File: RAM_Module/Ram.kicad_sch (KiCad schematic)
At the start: 10 parts, among them SW3 SW_Push, U3 74LS00, U4 74LS157, U5 74F189SC, U6 74F189SC, U7 74LS157, U8 74LS157

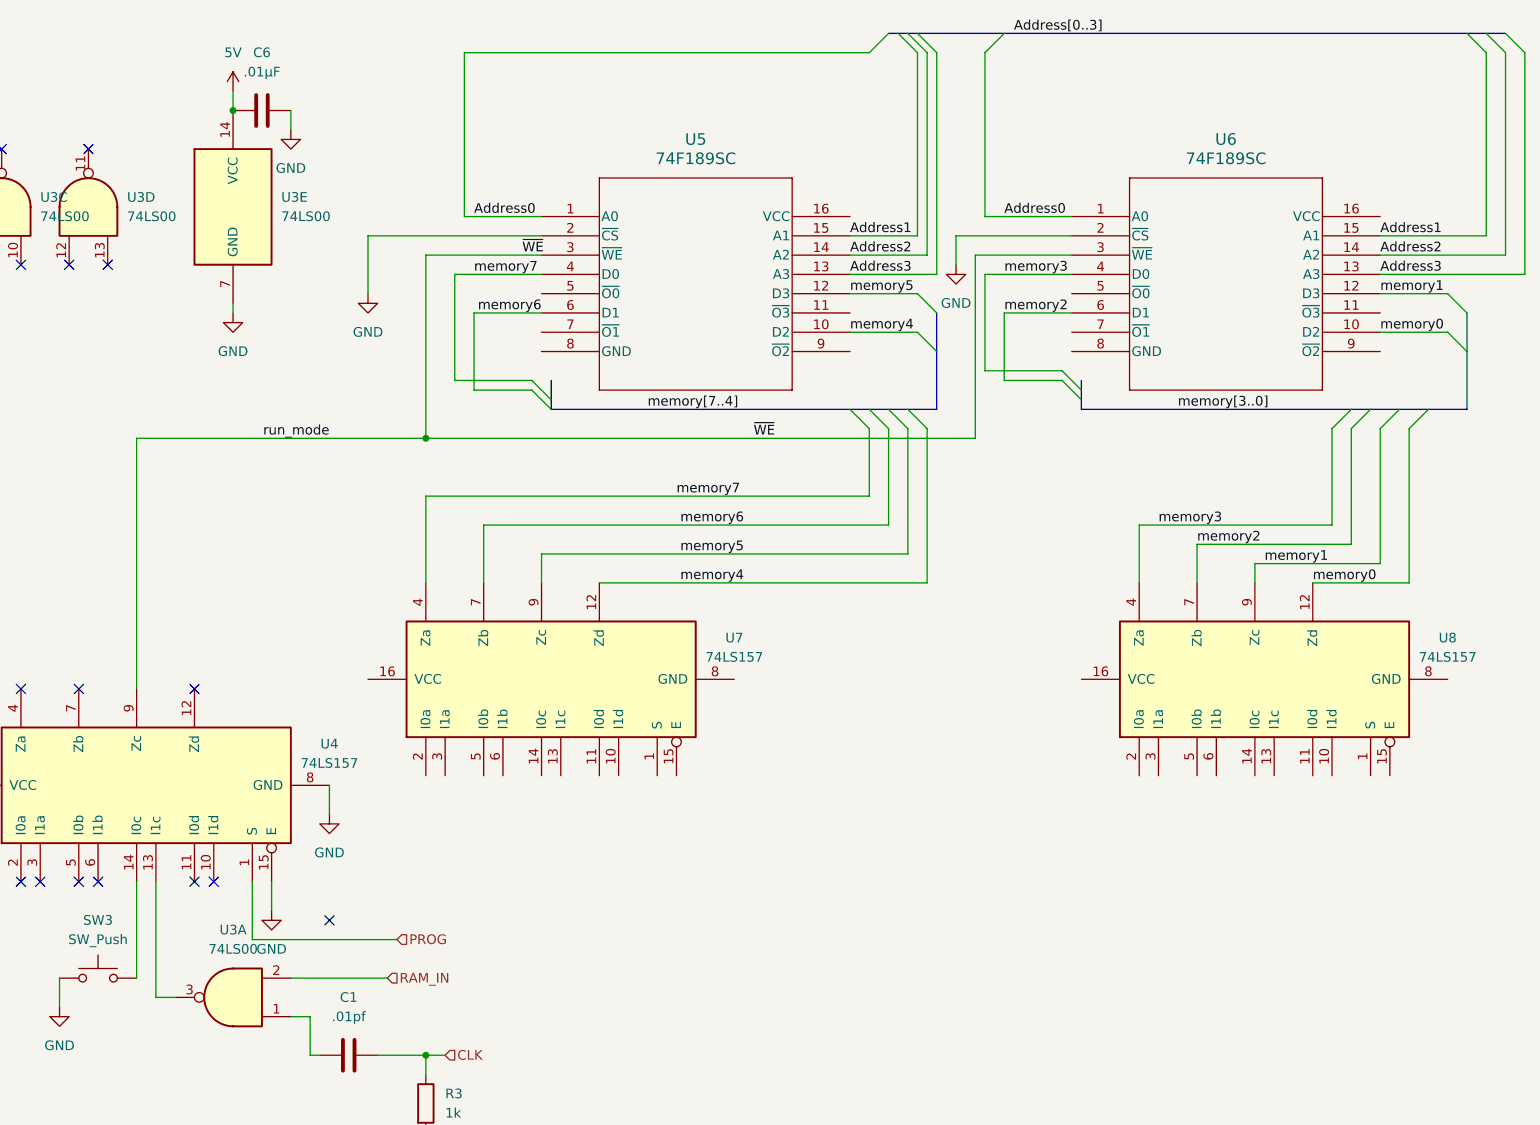
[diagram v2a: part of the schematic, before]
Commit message: updated RAM, changed bus alignment in ALU, RAM, and registers
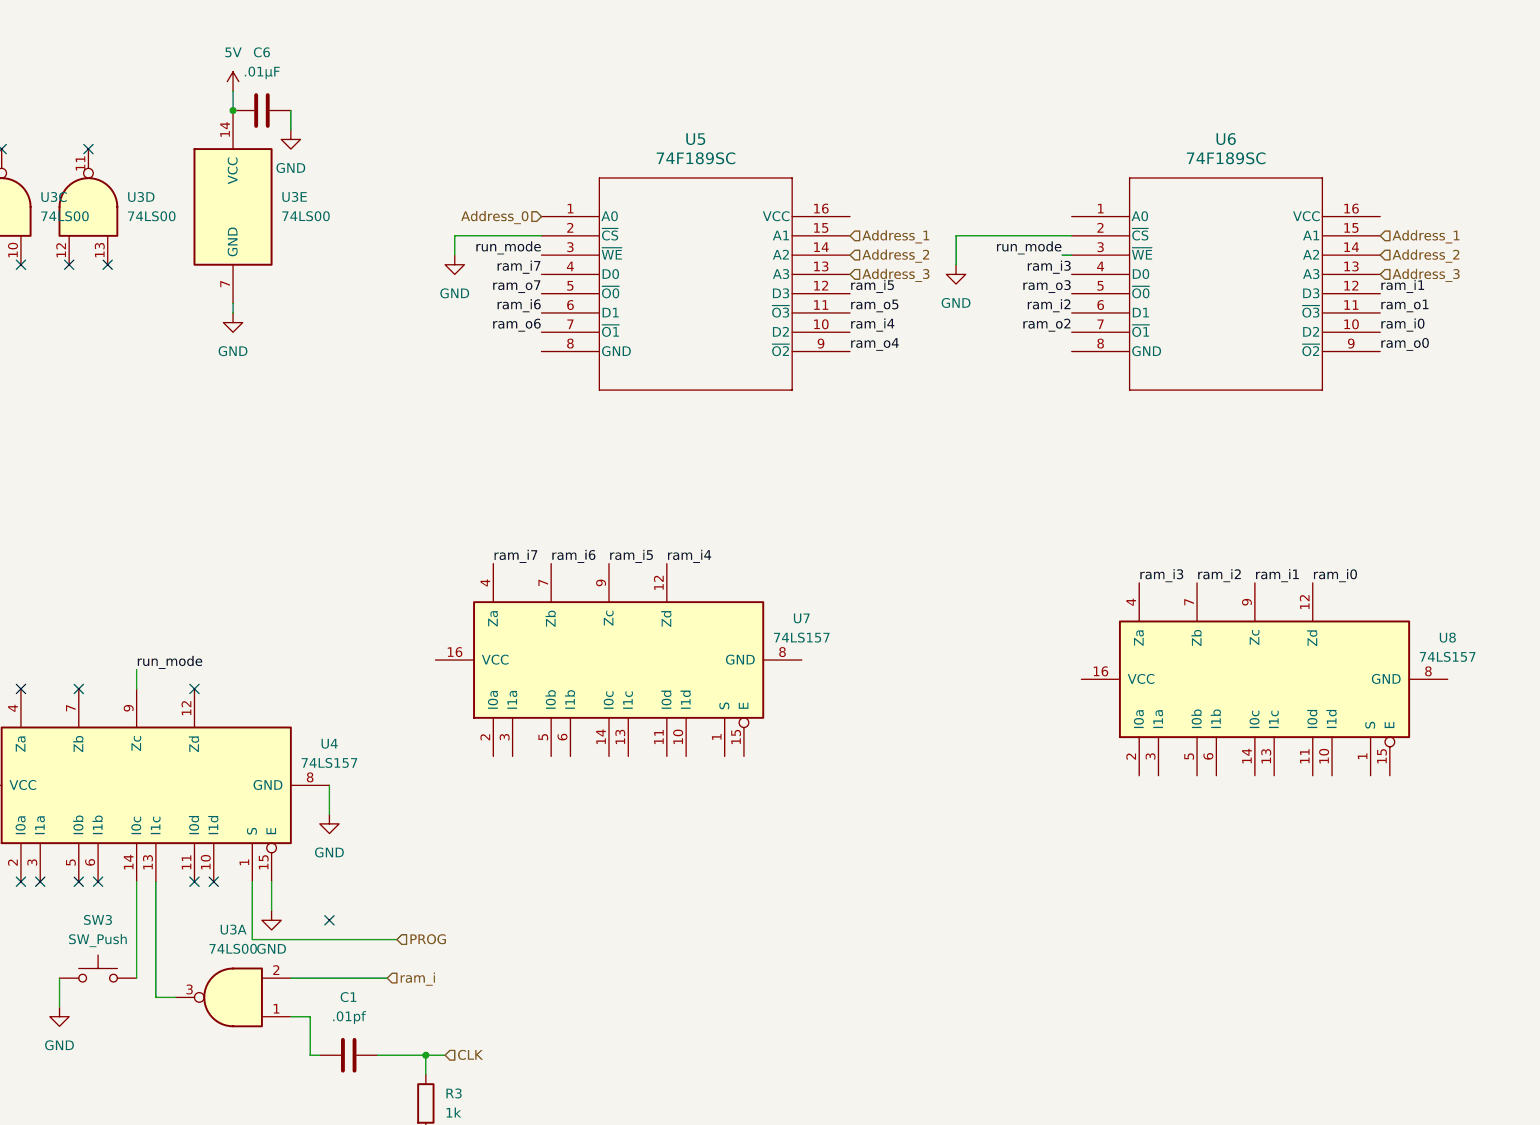
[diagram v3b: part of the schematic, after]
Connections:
- net ram_o5: now reaches U5.11 (~{O3})
- net ram_o7: now reaches U5.5 (~{O0})
- net ram_o6: now reaches U5.7 (~{O1})
- net ram_o4: now reaches U5.9 (~{O2})
- net ram_o1: now reaches U6.11 (~{O3})
- net ram_o3: now reaches U6.5 (~{O0})
- net ram_o2: now reaches U6.7 (~{O1})
- net ram_o0: now reaches U6.9 (~{O2})
- net Address0: no longer names the net of U6.1 (A0)
- net Address0: no longer U5.1 (A0)
- net Address1 renamed Address_1
- net Address2 renamed Address_2
- net Address3 renamed Address_3
- net RAM_IN renamed ram_i
- net memory0 renamed ram_i0
- net memory1 renamed ram_i1
- net memory2 renamed ram_i2
- net memory3 renamed ram_i3
- net memory4 renamed ram_i4
- net memory5 renamed ram_i5
- net memory6 renamed ram_i6
- net memory7 renamed ram_i7
- new net Address_0: U5.1 (A0)
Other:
- moved on the sheet: U7

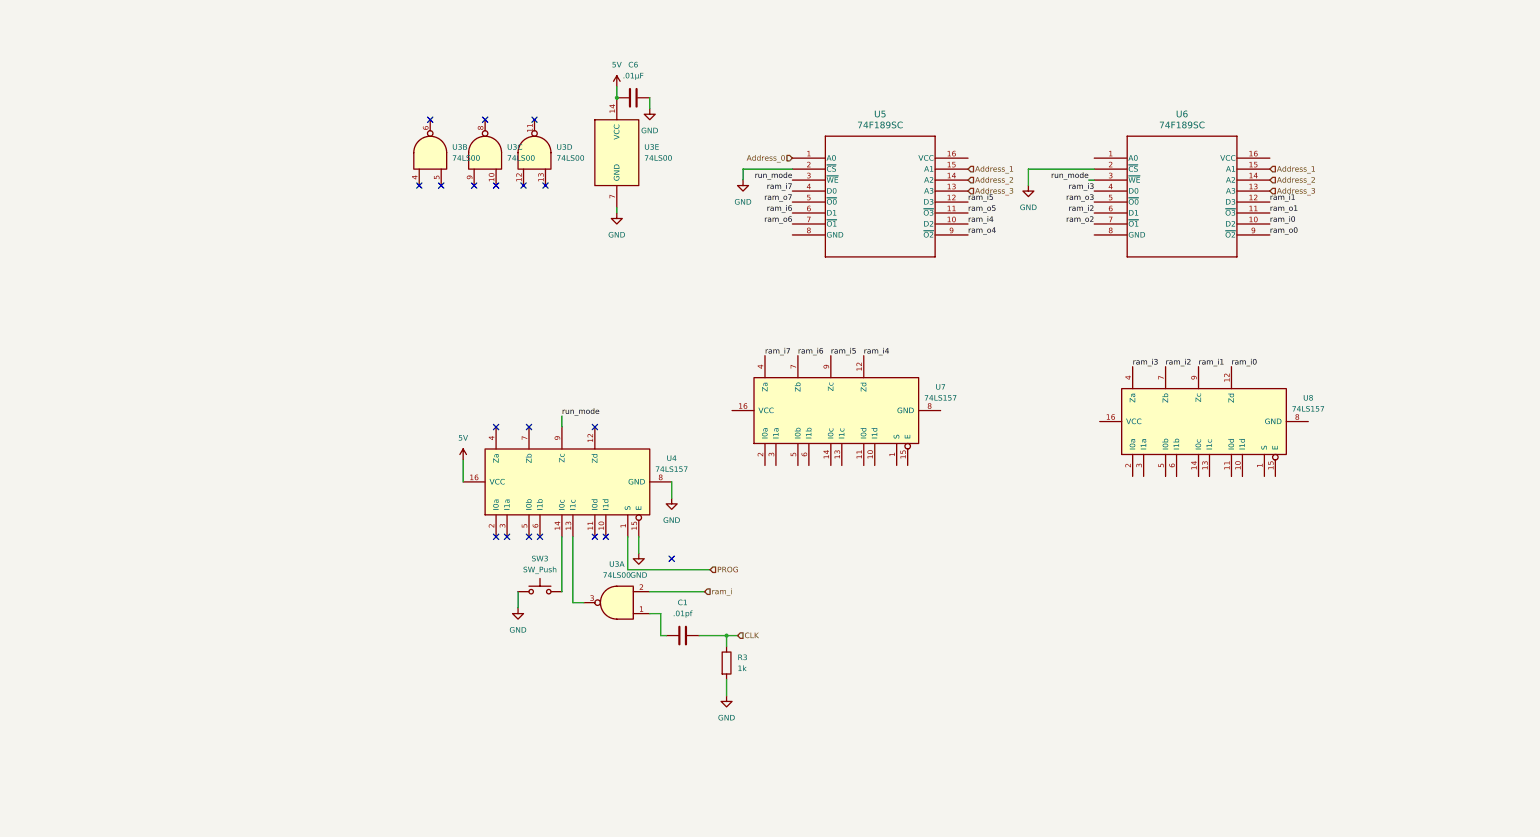
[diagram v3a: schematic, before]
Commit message: connected RAM
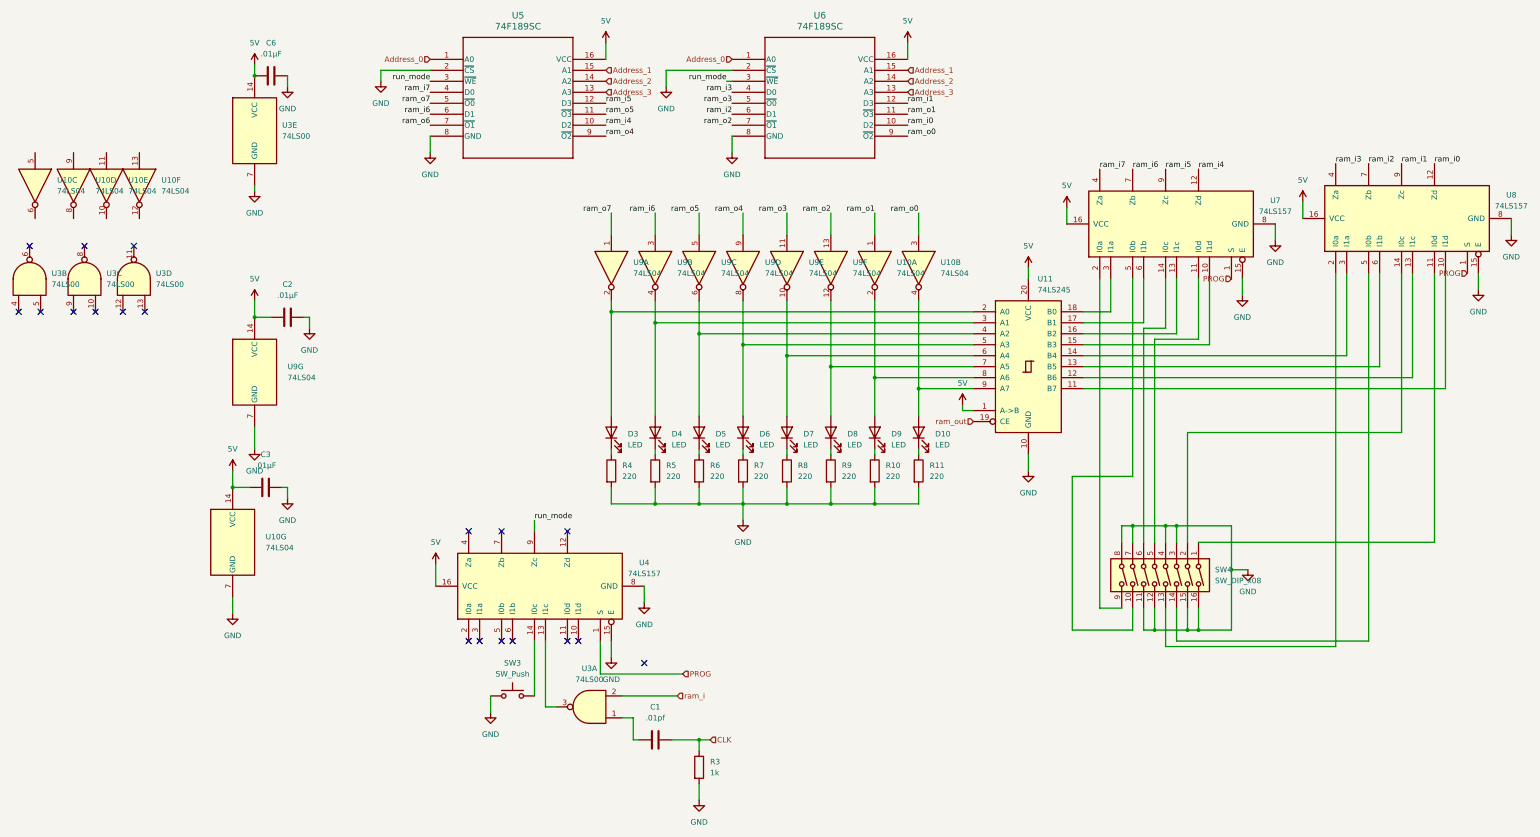
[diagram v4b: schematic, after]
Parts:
- added C2, C3: .01µF, Capacitor_THT:C_Disc_D5.0mm_W2.5mm_P2.50mm, symbol Device:C
- added D10, D3, D4, D5, D6, D7, D8, D9: LED, symbol Device:LED
- added R10, R11, R4, R5, R6, R7, R8, R9: 220, symbol Device:R
- added SW4: SW_DIP_x08, symbol Switch:SW_DIP_x08
- added U10, U9: 74LS04, symbol 74xx:74LS04
- added U11: 74LS245, symbol 74xx:74LS245
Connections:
- net 5V: now also U5.16 (VCC), U6.16 (VCC), U7.16 (VCC), U8.16 (VCC), C2.2, C3.2, U10.14 (VCC), U11.1 (A->B), U11.20 (VCC), U9.14 (VCC)
- net Address_0: now also U6.1 (A0)
- net GND: now also U5.8 (GND), U6.8 (GND), U7.15 (E), U7.8 (GND), U8.15 (E), U8.8 (GND), C2.1, C3.1, R10.2, R11.2, R4.2, R5.2, R6.2, R7.2, R8.2, R9.2, SW4.11, SW4.12, SW4.15, SW4.16, SW4.3, SW4.4, SW4.7, SW4.8, U10.7 (GND), U11.10 (GND), U9.7 (GND)
- net PROG: now also U7.1 (S), U8.1 (S)
- net ram_i6: now also U9.3
- net ram_o0: now also U10.3
- net ram_o1: now also U10.1
- net ram_o2: now also U9.13
- net ram_o3: now also U9.11
- net ram_o4: now also U9.9
- net ram_o5: now also U9.5
- net ram_o7: now also U9.1
- net at U7.10 (I1d): now also U11.15 (B3)
- net at U7.11 (I0d): now also SW4.5
- net at U7.13 (I1c): now also U11.16 (B2)
- net at U7.14 (I0c): now also SW4.6
- net at U7.2 (I0a): now also SW4.9
- net at U7.3 (I1a): now also U11.18 (B0)
- net at U7.5 (I0b): now also SW4.10
- net at U7.6 (I1b): now also U11.17 (B1)
- net at U8.10 (I1d): now also U11.11 (B7)
- net at U8.11 (I0d): now also SW4.1
- net at U8.13 (I1c): now also U11.12 (B6)
- net at U8.14 (I0c): now also SW4.2
- net at U8.2 (I0a): now also SW4.13
- net at U8.3 (I1a): now also U11.14 (B4)
- net at U8.5 (I0b): now also SW4.14
- net at U8.6 (I1b): now also U11.13 (B5)
- new net: D3.2 (A), U11.2 (A0), U9.2
- new net: D7.1 (K), R8.1
- new net: D7.2 (A), U11.6 (A4), U9.10
- new net: D4.1 (K), R5.1
- new net: D4.2 (A), U11.3 (A1), U9.4
- new net: D10.2 (A), U10.4, U11.9 (A7)
- new net: D9.1 (K), R10.1
- new net: D9.2 (A), U10.2, U11.8 (A6)
- new net: D10.1 (K), R11.1
- new net: D5.2 (A), U11.4 (A2), U9.6
- new net: D6.2 (A), U11.5 (A3), U9.8
- new net: D8.2 (A), U11.7 (A5), U9.12
- new net: D5.1 (K), R6.1
- new net: D3.1 (K), R4.1
- new net: D6.1 (K), R7.1
- new net: D8.1 (K), R9.1
- new net ram_out: U11.19 (CE)
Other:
- moved on the sheet: C1, C6, R3, SW3, U3A, U3B, U3C, U3D, U3E, U4, U5, U6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

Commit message: fixed Ram register, fixed mar in ram.v, updated caps in alu, ram, and instruction register
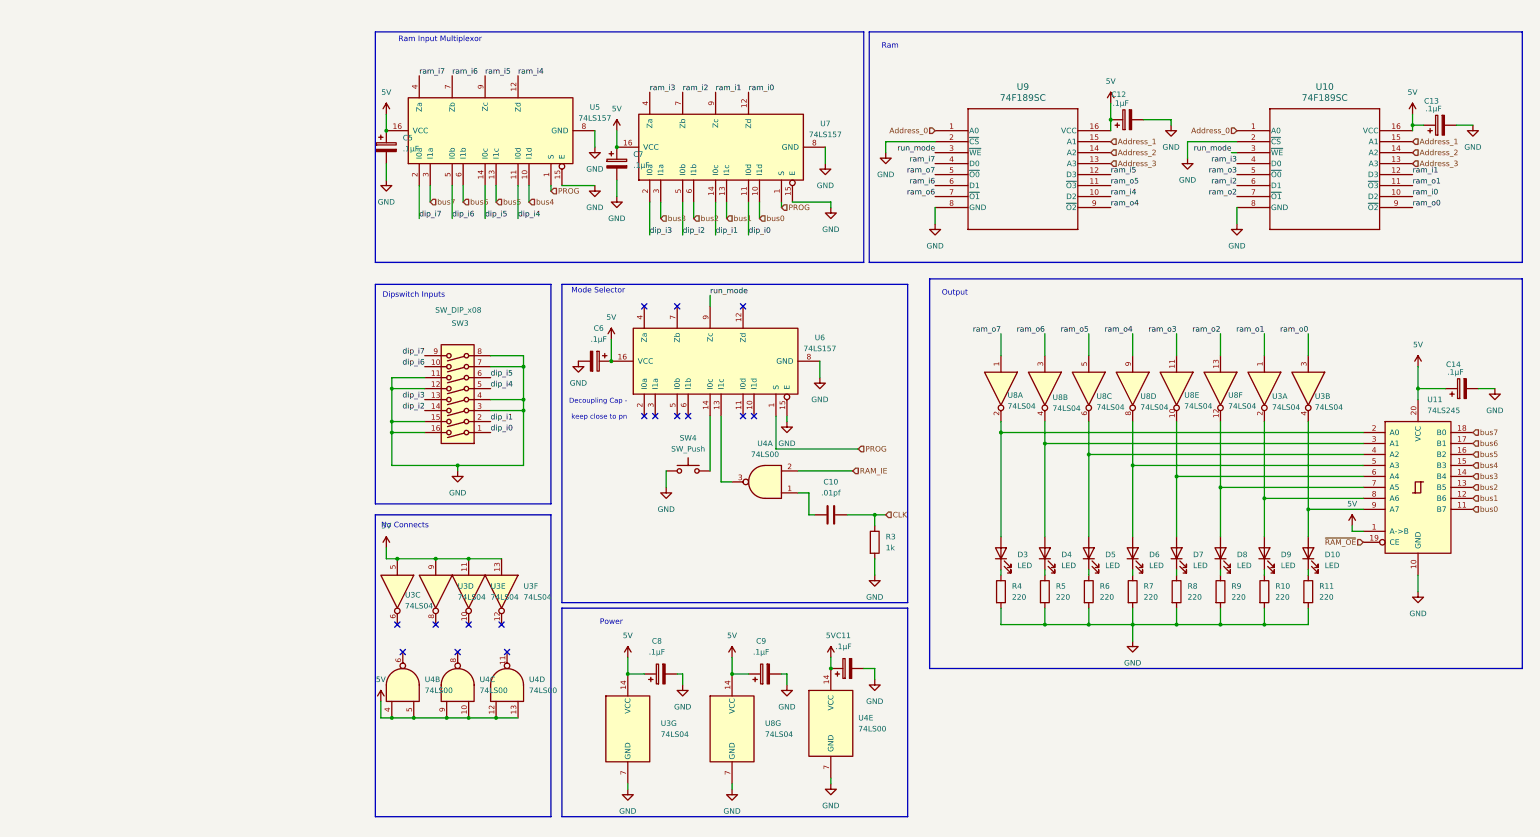
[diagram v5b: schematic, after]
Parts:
- removed C2, C3, C6: .01µF, Capacitor_THT:C_Disc_D5.0mm_W2.5mm_P2.50mm, symbol Device:C
- added C11, C12, C13, C14, C5, C6, C7, C8, C9: .1µF, symbol Device:C_Polarized
- renumbered C1 to C10, SW4 to SW3, SW3 to SW4, U6 to U10, U10 to U3, U3 to U4, U7 to U5, U4 to U6, U8 to U7, U9 to U8, U5 to U9
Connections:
- net 5V: now also U3.11, U3.13, U3.5, U3.9, U4.10, U4.12, U4.13, U4.4, U4.5, U4.9, C11.1, C12.1, C13.1, C14.1, C5.1, C6.1, C7.1, C8.1, C9.1
- net GND: now also C11.2, C12.2, C13.2, C14.2, C5.2, C6.2, C7.2, C8.2, C9.2
- net ram_i6: no longer U8.3
- net ram_o6: now also U8.3
- net bus4: now reaches U11.15 (B3), U5.10 (I1d)
- net dip_i4: now reaches SW3.5, U5.11 (I0d)
- net bus5: now reaches U11.16 (B2), U5.13 (I1c)
- net dip_i5: now reaches SW3.6, U5.14 (I0c)
- net dip_i7: now reaches SW3.9, U5.2 (I0a)
- net bus7: now reaches U11.18 (B0), U5.3 (I1a)
- net dip_i6: now reaches SW3.10, U5.5 (I0b)
- net bus6: now reaches U11.17 (B1), U5.6 (I1b)
- net bus0: now reaches U11.11 (B7), U7.10 (I1d)
- net dip_i0: now reaches SW3.1, U7.11 (I0d)
- net bus1: now reaches U11.12 (B6), U7.13 (I1c)
- net dip_i1: now reaches SW3.2, U7.14 (I0c)
- net dip_i3: now reaches SW3.13, U7.2 (I0a)
- net bus3: now reaches U11.14 (B4), U7.3 (I1a)
- net dip_i2: now reaches SW3.14, U7.5 (I0b)
- net bus2: now reaches U11.13 (B5), U7.6 (I1b)
- net ram_i renamed RAM_IE
- net ram_out renamed ~{RAM_OE}
- no-connect marks 19 -> 16
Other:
- note added: "Decoupling Cap - keep close to pn"
- note added: "Dipswitch Inputs"
- note added: "Mode Selector"
- note added: "No Connects"
- note added: "Output"
- note added: "Power"
- note added: "Ram"
- note added: "Ram Input Multiplexor"
- moved on the sheet: C10, D10, D3, D4, D5, D6, D7, D8, D9, R10, R11, R3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

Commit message: Added Program Counter Schematic
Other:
- company: (none) -> Arsenal Gear
- title: (none) -> Ram Module
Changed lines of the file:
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@@
 	(generator_version "9.0")
 	(paper "A4")
+	(title_block
+		(title "Ram Module")
+		(date "2025-08-25")
+		(company "Arsenal Gear")
+	)
 	(rectangle
 		(start 13.97 127)
